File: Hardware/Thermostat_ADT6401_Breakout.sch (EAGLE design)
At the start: 26 parts, among them Q1 20V/4.2A/52mΩ/1.4W, SW1 DIP-06, U1 ADT6401

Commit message: Update SPDT chart pt 2
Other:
- note added: "1"
- note added: "1 0 x 1 0 x 1 0 x 1 0 x 1 0 x 1 0 x 1 0 x 1 0 x 1 0 x"
- note added: "1 1 0 1 1 0 1 1 0 1 1 0 1 1 0 1 1 0 1 1 0 1 1 0 1 1 0"
- note added: "1 1 1 0 0 0 x x x 1 1 1 0 0 0 x x x 1 1 1 0 0 0 x x x"
- note added: "1 1 1 1 1 1 0 0 0 1 1 1 1 1 1 0 0 0 1 1 1 1 1 1 0 0 0"
- note added: "1 1 1 1 1 1 1 1 1 0 0 0 0 0 0 0 0 0 x x x x x x x x x"
- note added: "1 1 1 1 1 1 1 1 1 1 1 1 1 1 1 1 1 1 0 0 0 0 0 0 0 0 0"
- note added: "2"
- note added: "3"
- note added: "4"
- note added: "5"
- note added: "6"

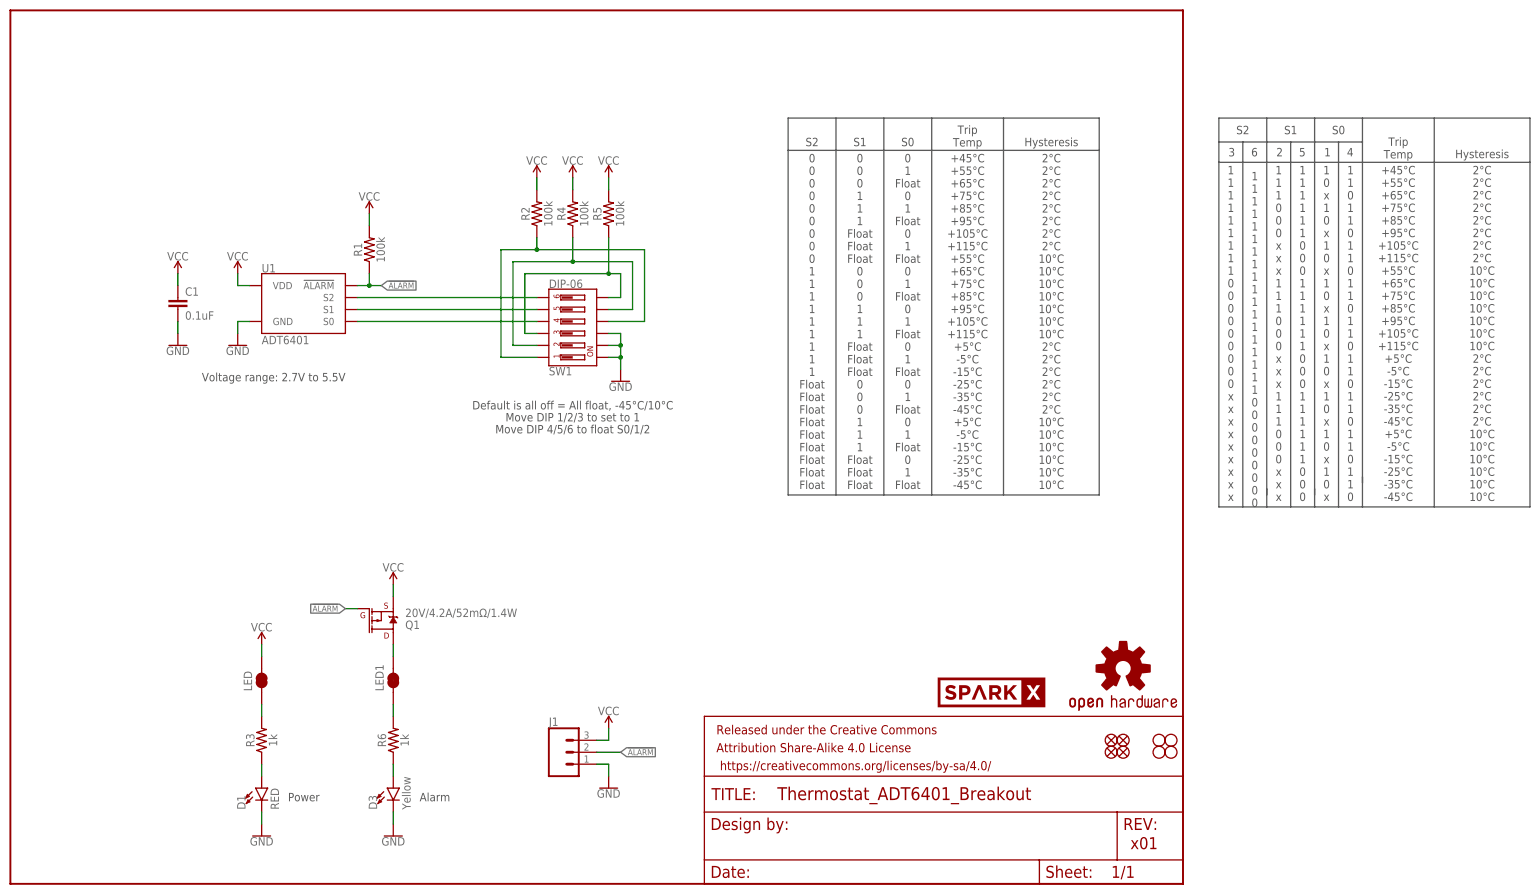
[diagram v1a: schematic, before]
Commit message: Combine switches into chart. Add ignore. Remove old files.
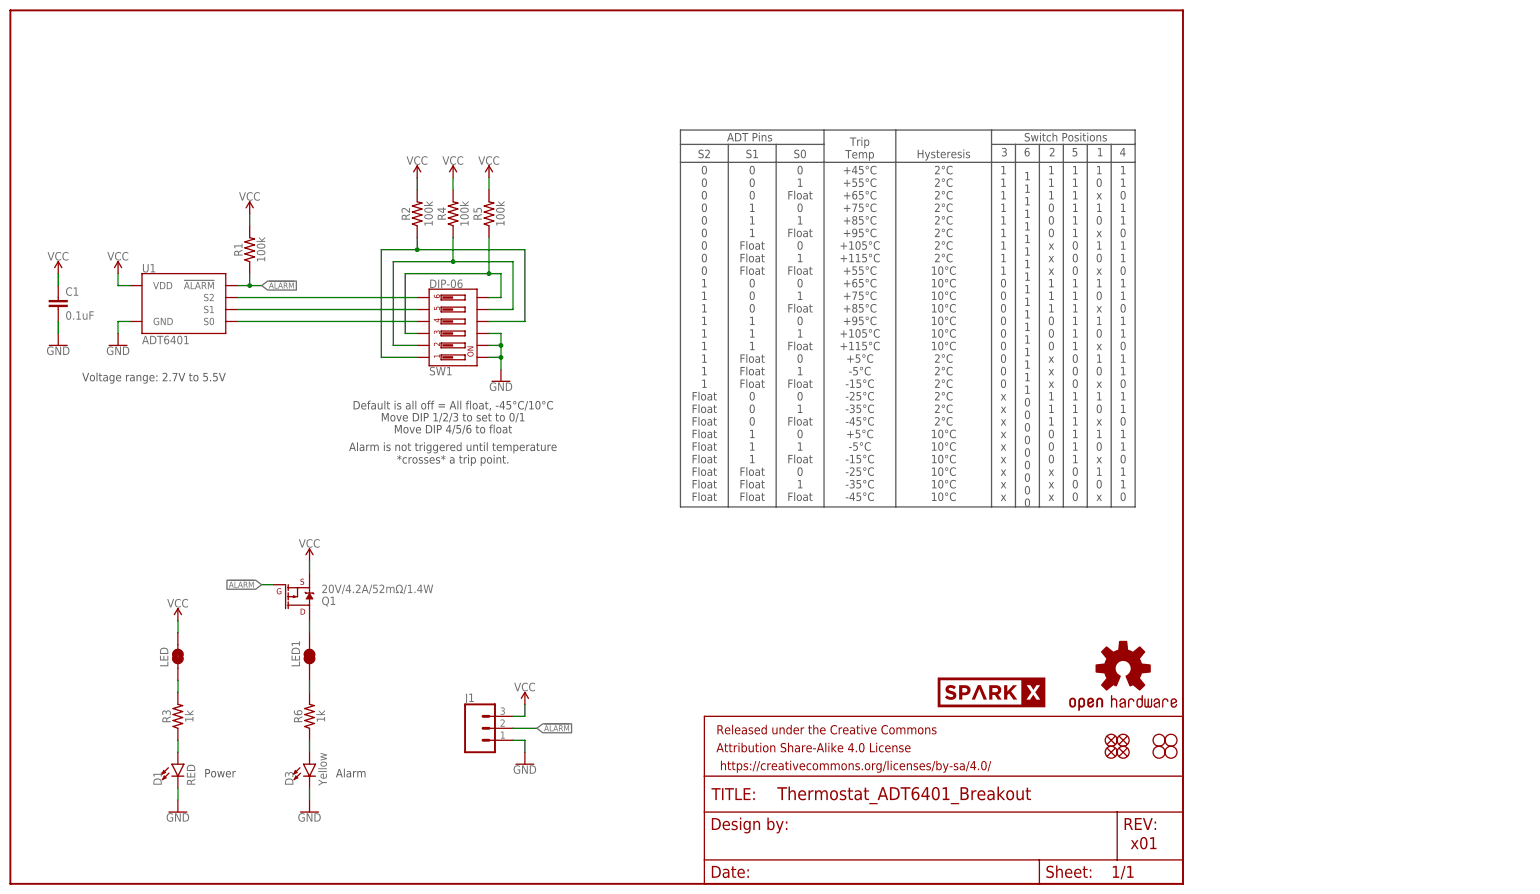
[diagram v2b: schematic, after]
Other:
- note added: "ADT Pins"
- note added: "Alarm is not triggered until temperature *crosses* a trip point."
- note added: "Move DIP 1/2/3 to set to 0/1"
- note added: "Move DIP 4/5/6 to float"
- note added: "Switch Positions"
- note removed: "Move DIP 1/2/3 to set to 1"
- note removed: "Move DIP 4/5/6 to float S0/1/2"
- moved on the sheet: C1, D1, D3, J1, LED, LED1, Q1, R1, R2, R3, R4, R5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
